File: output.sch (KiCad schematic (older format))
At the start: 12 parts, among them U3 OPA549, U4 INA240A1D, U5 OPA549, U6 INA240A1D

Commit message: Finished first version of schematic
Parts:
- removed R10: R_Shunt, symbol Device:R_Shunt
- added R17: R_Shunt, Resistor_SMD:R_Shunt_Ohmite_LVK12, symbol Device:R_Shunt
- C7: renamed from C14; footprint (none) -> Capacitor_SMD:C_0603_1608Metric
- C8: renamed from C15; footprint (none) -> Capacitor_SMD:C_0603_1608Metric
- R12: renamed from R5; footprint (none) -> Resistor_SMD:R_0603_1608Metric
- R13: renamed from R6; footprint (none) -> Resistor_SMD:R_0603_1608Metric
- R14: renamed from R7; footprint (none) -> Resistor_SMD:R_Shunt_Ohmite_LVK12; OrderN (none) -> LVK12R010DERCT-ND
- R15: renamed from R8; footprint (none) -> Resistor_SMD:R_0603_1608Metric
- R16: renamed from R9; footprint (none) -> Resistor_SMD:R_0603_1608Metric
- renumbered U3 to U1, U4 to U2, U5 to U3, U6 to U4
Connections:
- net SENSE_4T_1: now also R17.4
- net SENSE_4T_2: now also R17.1
- net at U4.1 (-): now also R17.3
- net at U4.8 (+): now also R17.2
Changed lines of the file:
@@
 $Descr A4 11693 8268
 encoding utf-8
-Sheet 3 4
-Title ""
-Date ""
-Rev ""
-Comp ""
+Sheet 2 5
+Title "Z Sim"
+Date "2019-10-22"
+Rev "0.1"
+Comp "ELp"
 Comment1 ""
 Comment2 ""
@@
 $EndDescr
 $Comp
-L rise_elp:OPA549 U3
+L rise_elp:OPA549 U1
 U 1 1 5DADB292
 P 2500 3250
-F 0 "U3" H 2750 3550 50  0000 L CNN
+F 0 "U1" H 2750 3550 50  0000 L CNN
 F 1 "OPA549" H 2400 3250 50  0000 L CNN
 F 2 "Package_TO_SOT_THT:TO-220-11_P3.4x5.08mm_StaggerOdd_Lead4.85mm_Vertical" H 2500 3250 50  0001 C CNN
@@
 	2450 2600 2450 2800
 $Comp
-L power:GND #PWR0120
+L power:GND #PWR014
 U 1 1 5DADB93D
 P 2450 4250
-F 0 "#PWR0120" H 2450 4000 50  0001 C CNN
+F 0 "#PWR014" H 2450 4000 50  0001 C CNN
 F 1 "GND" H 2455 4077 50  0000 C CNN
 F 2 "" H 2450 4250 50  0001 C CNN
@@
 V_OUT1
 $Comp
-L Device:R_Small R6
+L Device:R_Small R13
 U 1 1 5DADC336
 P 1400 3450
-F 0 "R6" H 1459 3496 50  0000 L CNN
+F 0 "R13" H 1459 3496 50  0000 L CNN
 F 1 "10k" H 1459 3405 50  0000 L CNN
-F 2 "" H 1400 3450 50  0001 C CNN
+F 2 "Resistor_SMD:R_0603_1608Metric" H 1400 3450 50  0001 C CNN
 F 3 "~" H 1400 3450 50  0001 C CNN
 	1    1400 3450
@@
 $EndComp
 $Comp
-L Device:R_Small R5
+L Device:R_Small R12
 U 1 1 5DADCC5D
 P 1400 2700
-F 0 "R5" H 1459 2746 50  0000 L CNN
+F 0 "R12" H 1459 2746 50  0000 L CNN
 F 1 "10k" H 1459 2655 50  0000 L CNN
-F 2 "" H 1400 2700 50  0001 C CNN
+F 2 "Resistor_SMD:R_0603_1608Metric" H 1400 2700 50  0001 C CNN
 F 3 "~" H 1400 2700 50  0001 C CNN
 	1    1400 2700
@@
 ES1
 $Comp
-L Device:R_Shunt R7
+L Device:R_Shunt R14
 U 1 1 5DADFAE8
 P 3750 3200
-F 0 "R7" V 3525 3200 50  0000 C CNN
+F 0 "R14" V 3525 3200 50  0000 C CNN
 F 1 "R_Shunt" V 3616 3200 50  0000 C CNN
-F 2 "" V 3680 3200 50  0001 C CNN
+F 2 "Resistor_SMD:R_Shunt_Ohmite_LVK12" V 3680 3200 50  0001 C CNN
 F 3 "~" H 3750 3200 50  0001 C CNN
+F 4 "LVK12R010DERCT-ND" V 3750 3200 50  0001 C CNN "OrderN"
 	1    3750 3200
 	0    1    1    0
@@
 	3350 3300 3150 3300
 $Comp
-L Amplifier_Current:INA240A1D U4
+L Amplifier_Current:INA240A1D U2
 U 1 1 5DAE1093
 P 3750 3900
-F 0 "U4" V 3750 4050 50  0000 L CNN
+F 0 "U2" V 3750 4050 50  0000 L CNN
 F 1 "INA240A1D" V 3850 4050 50  0000 L CNN
 F 2 "Package_SO:SOIC-8_3.9x4.9mm_P1.27mm" H 3750 3250 50  0001 C CNN
@@
 	3350 3800 3450 3800
 $Comp
-L power:GND #PWR0121
+L power:GND #PWR015
 U 1 1 5DAE8C45
 P 3350 4100
-F 0 "#PWR0121" H 3350 3850 50  0001 C CNN
+F 0 "#PWR015" H 3350 3850 50  0001 C CNN
 F 1 "GND" H 3355 3927 50  0000 C CNN
 F 2 "" H 3350 4100 50  0001 C CNN
@@
 Connection ~ 4250 3500
 $Comp
-L Device:C_Small C14
+L Device:C_Small C7
 U 1 1 5DAE9B2D
 P 3150 3850
-F 0 "C14" H 3000 3750 50  0000 L CNN
+F 0 "C7" H 3000 3750 50  0000 L CNN
 F 1 "2.2u" H 2950 3950 50  0000 L CNN
-F 2 "" H 3150 3850 50  0001 C CNN
+F 2 "Capacitor_SMD:C_0603_1608Metric" H 3150 3850 50  0001 C CNN
 F 3 "~" H 3150 3850 50  0001 C CNN
 	1    3150 3850
@@
 Connection ~ 3250 3500
 $Comp
-L power:+3.3VA #PWR0122
+L power:+3.3VA #PWR016
 U 1 1 5DAE93D3
 P 4250 3400
-F 0 "#PWR0122" H 4250 3250 50  0001 C CNN
+F 0 "#PWR016" H 4250 3250 50  0001 C CNN
 F 1 "+3.3VA" H 4050 3450 50  0000 C CNN
 F 2 "" H 4250 3400 50  0001 C CNN
@@
 	5750 3200 5550 3200
 $Comp
-L power:GND #PWR0123
+L power:GND #PWR017
 U 1 1 5DAEEBB5
 P 6450 4250
-F 0 "#PWR0123" H 6450 4000 50  0001 C CNN
+F 0 "#PWR017" H 6450 4000 50  0001 C CNN
 F 1 "GND" H 6455 4077 50  0000 C CNN
 F 2 "" H 6450 4250 50  0001 C CNN
@@
 	6350 2850 6350 2600
 $Comp
-L rise_elp:OPA549 U5
+L rise_elp:OPA549 U3
 U 1 1 5DAEEBCF
 P 6400 3250
-F 0 "U5" H 6650 3550 50  0000 L CNN
+F 0 "U3" H 6650 3550 50  0000 L CNN
 F 1 "OPA549" H 6300 3250 50  0000 L CNN
 F 2 "Package_TO_SOT_THT:TO-220-11_P3.4x5.08mm_StaggerOdd_Lead4.85mm_Vertical" H 6400 3250 50  0001 C CNN
@@
 	6450 4250 6450 4100
 $Comp
-L Device:R_Small R9
+L Device:R_Small R16
 U 1 1 5DAEEBA7
 P 7450 3450
-F 0 "R9" H 7509 3496 50  0000 L CNN
+F 0 "R16" H 7509 3496 50  0000 L CNN
 F 1 "10k" H 7509 3405 50  0000 L CNN
-F 2 "" H 7450 3450 50  0001 C CNN
+F 2 "Resistor_SMD:R_0603_1608Metric" H 7450 3450 50  0001 C CNN
 F 3 "~" H 7450 3450 50  0001 C CNN
 	1    7450 3450
@@
 $EndComp
 $Comp
-L Device:R_Small R8
+L Device:R_Small R15
 U 1 1 5DAEEB41
 P 7450 2700
-F 0 "R8" H 7509 2746 50  0000 L CNN
+F 0 "R15" H 7509 2746 50  0000 L CNN
 F 1 "10k" H 7509 2655 50  0000 L CNN
-F 2 "" H 7450 2700 50  0001 C CNN
+F 2 "Resistor_SMD:R_0603_1608Metric" H 7450 2700 50  0001 C CNN
 F 3 "~" H 7450 2700 50  0001 C CNN
 	1    7450 2700
@@
 	9000 3500 9000 3300
 $Comp
-L power:GND #PWR0124
+L power:GND #PWR018
 U 1 1 5DAF9612
 P 9000 3600
-F 0 "#PWR0124" H 9000 3350 50  0001 C CNN
+F 0 "#PWR018" H 9000 3350 50  0001 C CNN
 F 1 "GND" H 9005 3427 50  0000 C CNN
 F 2 "" H 9000 3600 50  0001 C CNN
@@
 	9000 3300 9100 3300
 $Comp
-L Amplifier_Current:INA240A1D U6
+L Amplifier_Current:INA240A1D U4
 U 1 1 5DAF962B
 P 9400 3400
-F 0 "U6" V 9400 3550 50  0000 L CNN
+F 0 "U4" V 9400 3550 50  0000 L CNN
 F 1 "INA240A1D" V 9500 3550 50  0000 L CNN
 F 2 "Package_SO:SOIC-8_3.9x4.9mm_P1.27mm" H 9400 2750 50  0001 C CNN
@@
 	9100 3400 8900 3400
 $Comp
-L Device:C_Small C15
+L Device:C_Small C8
 U 1 1 5DAF963B
 P 8800 3350
-F 0 "C15" H 8650 3250 50  0000 L CNN
+F 0 "C8" H 8650 3250 50  0000 L CNN
 F 1 "2.2u" H 8600 3450 50  0000 L CNN
-F 2 "" H 8800 3350 50  0001 C CNN
+F 2 "Capacitor_SMD:C_0603_1608Metric" H 8800 3350 50  0001 C CNN
 F 3 "~" H 8800 3350 50  0001 C CNN
 	1    8800 3350
@@
 Wire Wire Line
 	9900 2900 9900 3000
-$Comp
-L Device:R_Shunt R10
-U 1 1 5DAF964D
-P 9400 2700
-F 0 "R10" V 9175 2700 50  0000 C CNN
-F 1 "R_Shunt" V 9266 2700 50  0000 C CNN
-F 2 "" V 9330 2700 50  0001 C CNN
-F 3 "~" H 9400 2700 50  0001 C CNN
-	1    9400 2700
-	0    1    1    0
-$EndComp
 Wire Wire Line
 	8900 3400 8900 3000
 $Comp
-L power:+3.3VA #PWR0125
+L power:+3.3VA #PWR019
 U 1 1 5DB044D1
 P 9900 2900
-F 0 "#PWR0125" H 9900 2750 50  0001 C CNN
+F 0 "#PWR019" H 9900 2750 50  0001 C CNN
 F 1 "+3.3VA" H 9700 2950 50  0000 C CNN
 F 2 "" H 9900 2900 50  0001 C CNN
@@
 Text HLabel 9600 2700 2    50   Input ~ 0
 SENSE_4T_2
+$Comp
+L Device:R_Shunt R17
+U 1 1 5DAEC8CF
+P 9400 2700
+F 0 "R17" V 9175 2700 50  0000 C CNN
+F 1 "R_Shunt" V 9266 2700 50  0000 C CNN
+F 2 "Resistor_SMD:R_Shunt_Ohmite_LVK12" V 9330 2700 50  0001 C CNN
+F 3 "~" H 9400 2700 50  0001 C CNN
+F 4 "LVK12R010DERCT-ND" V 9400 2700 50  0001 C CNN "OrderN"
+	1    9400 2700
+	0    1    1    0
+$EndComp
 $EndSCHEMATC

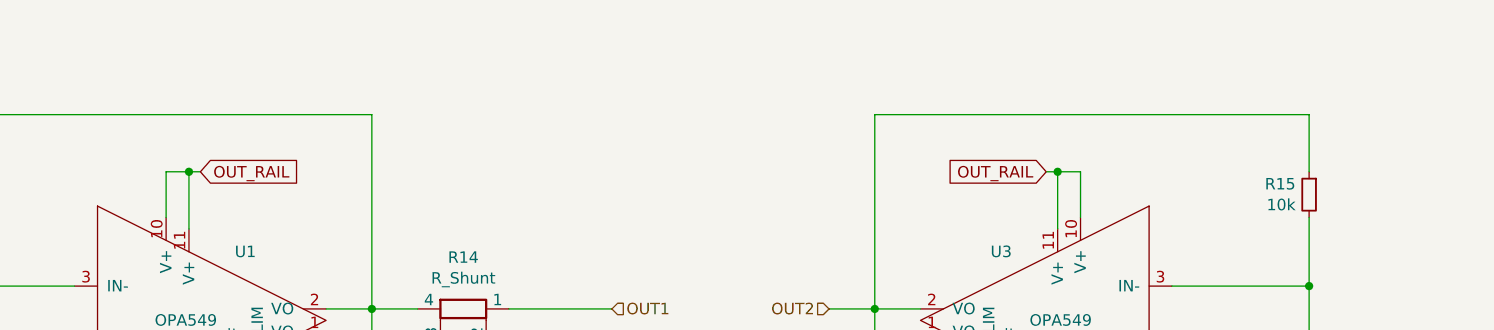
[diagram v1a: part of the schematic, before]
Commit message: preparation for routing and adding kylfläns
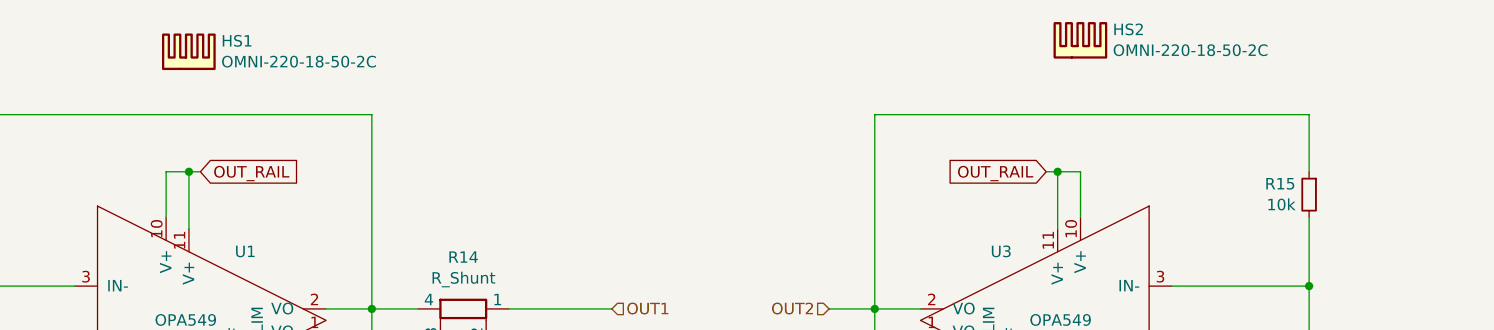
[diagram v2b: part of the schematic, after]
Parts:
- added HS1, HS2: OMNI-220-18-50-2C, rise_elp:OMNI-220-18-50-2C, symbol Mechanical:Heatsink
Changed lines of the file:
@@
 	0    1    1    0
 $EndComp
+$Comp
+L Mechanical:Heatsink HS1
+U 1 1 5DBA0CBC
+P 2550 2150
+F 0 "HS1" H 2691 2271 50  0000 L CNN
+F 1 "OMNI-220-18-50-2C" H 2691 2180 50  0000 L CNN
+F 2 "rise_elp:OMNI-220-18-50-2C" H 2562 2150 50  0001 C CNN
+F 3 "~" H 2562 2150 50  0001 C CNN
+F 4 "345-1491-ND" H 2550 2150 50  0001 C CNN "OrderN"
+	1    2550 2150
+	1    0    0    -1
+$EndComp
+$Comp
+L Mechanical:Heatsink HS2
+U 1 1 5DBA3198
+P 6450 2100
+F 0 "HS2" H 6591 2221 50  0000 L CNN
+F 1 "OMNI-220-18-50-2C" H 6591 2130 50  0000 L CNN
+F 2 "rise_elp:OMNI-220-18-50-2C" H 6462 2100 50  0001 C CNN
+F 3 "~" H 6462 2100 50  0001 C CNN
+F 4 "345-1491-ND" H 6450 2100 50  0001 C CNN "OrderN"
+	1    6450 2100
+	1    0    0    -1
+$EndComp
 $EndSCHEMATC

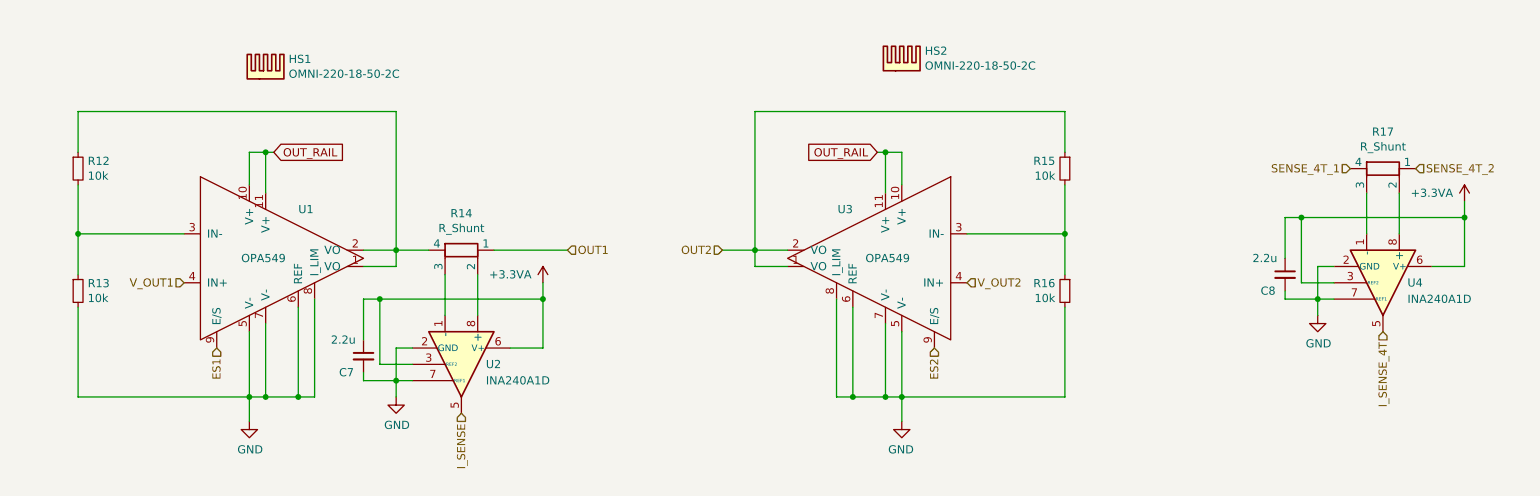
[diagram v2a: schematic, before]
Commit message: Schematic updates, added 3D models and started routing
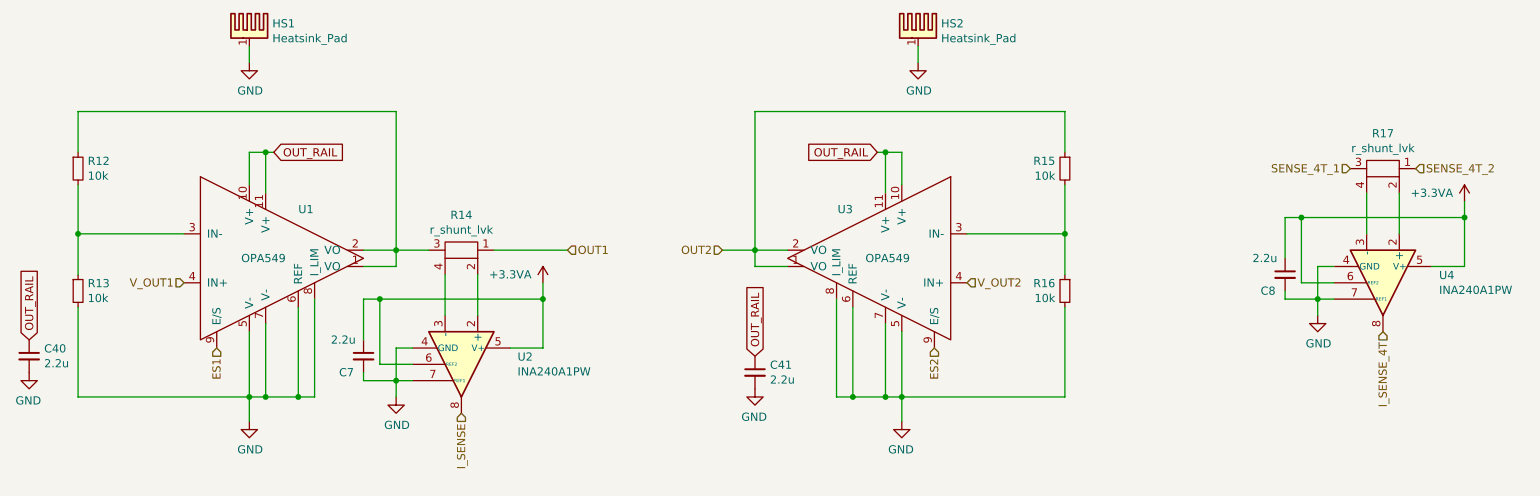
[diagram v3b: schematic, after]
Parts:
- removed HS1, HS2: OMNI-220-18-50-2C, rise_elp:OMNI-220-18-50-2C, symbol Mechanical:Heatsink
- removed R14, R17: R_Shunt, Resistor_SMD:R_Shunt_Ohmite_LVK12, symbol Device:R_Shunt
- removed U2, U4: INA240A1D, Package_SO:SOIC-8_3.9x4.9mm_P1.27mm, symbol Amplifier_Current:INA240A1D
- added C40, C41: 2.2u, Capacitor_SMD:C_0603_1608Metric, symbol Device:C_Small
- added HS1, HS2: Heatsink_Pad, rise_elp:OMNI-220-18-50-2C, symbol Mechanical:Heatsink_Pad
- added R14, R17: r_shunt_lvk, Resistor_SMD:R_Shunt_Ohmite_LVK12, symbol rise_elp:r_shunt_lvk
- added U2, U4: INA240A1PW, Package_SO:TSSOP-8_4.4x3mm_P0.65mm, symbol Amplifier_Current:INA240A1PW
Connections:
- net +3.3VA: now also U2.5 (V+), U2.6 (REF2), U4.5 (V+), U4.6 (REF2)
- net GND: now also C40.2, C41.2, HS1.1, HS2.1, U2.1 (GND), U2.4 (GND), U2.7 (REF1), U4.1 (GND), U4.4 (GND), U4.7 (REF1)
- net I_SENSE: now also U2.8
- net I_SENSE_4T: now also U4.8
- net OUT1: now also R14.1
- net OUT_RAIL: now also C40.1, C41.1
- net SENSE_4T_1: now also R17.3
- net SENSE_4T_2: now also R17.1
- net at R12.1, U1.1 (VO), U1.2 (VO): now also R14.3
- new net: R17.2, U4.2 (+)
- new net: R17.4, U4.3 (-)
- new net: R14.2, U2.2 (+)
- new net: R14.4, U2.3 (-)
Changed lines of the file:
@@
 Text HLabel 2250 3800 3    50   Input ~ 0
 ES1
-$Comp
-L Device:R_Shunt R14
-U 1 1 5DADFAE8
-P 3750 3200
-F 0 "R14" V 3525 3200 50  0000 C CNN
-F 1 "R_Shunt" V 3616 3200 50  0000 C CNN
-F 2 "Resistor_SMD:R_Shunt_Ohmite_LVK12" V 3680 3200 50  0001 C CNN
-F 3 "~" H 3750 3200 50  0001 C CNN
-F 4 "LVK12R010DERCT-ND" V 3750 3200 50  0001 C CNN "OrderN"
-	1    3750 3200
-	0    1    1    0
-$EndComp
 Wire Wire Line
 	3350 3200 3550 3200
@@
 Wire Wire Line
 	3350 3300 3150 3300
-$Comp
-L Amplifier_Current:INA240A1D U2
-U 1 1 5DAE1093
-P 3750 3900
-F 0 "U2" V 3750 4050 50  0000 L CNN
-F 1 "INA240A1D" V 3850 4050 50  0000 L CNN
-F 2 "Package_SO:SOIC-8_3.9x4.9mm_P1.27mm" H 3750 3250 50  0001 C CNN
-F 3 "http://www.ti.com/lit/ds/symlink/ina240.pdf" H 3900 4050 50  0001 C CNN
-F 4 "296-45088-1-ND" V 3750 3900 50  0001 C CNN "OrderN"
-	1    3750 3900
-	0    1    1    0
-$EndComp
 Wire Wire Line
 	3650 3600 3650 3350
@@
 Wire Wire Line
 	9000 3300 9100 3300
-$Comp
-L Amplifier_Current:INA240A1D U4
-U 1 1 5DAF962B
-P 9400 3400
-F 0 "U4" V 9400 3550 50  0000 L CNN
-F 1 "INA240A1D" V 9500 3550 50  0000 L CNN
-F 2 "Package_SO:SOIC-8_3.9x4.9mm_P1.27mm" H 9400 2750 50  0001 C CNN
-F 3 "http://www.ti.com/lit/ds/symlink/ina240.pdf" H 9550 3550 50  0001 C CNN
-F 4 "296-45088-1-ND" V 9400 3400 50  0001 C CNN "OrderN"
-	1    9400 3400
-	0    1    1    0
-$EndComp
 Wire Wire Line
 	9900 3300 9700 3300
@@
 SENSE_4T_2
 $Comp
-L Device:R_Shunt R17
-U 1 1 5DAEC8CF
+L Mechanical:Heatsink_Pad HS1
+U 1 1 5DB19FF5
+P 2450 1850
+F 0 "HS1" H 2591 1889 50  0000 L CNN
+F 1 "Heatsink_Pad" H 2591 1798 50  0000 L CNN
+F 2 "rise_elp:OMNI-220-18-50-2C" H 2462 1800 50  0001 C CNN
+F 3 "~" H 2462 1800 50  0001 C CNN
+F 4 "345-1491-ND" H 2450 1850 50  0001 C CNN "OrderN"
+	1    2450 1850
+	1    0    0    -1
+$EndComp
+$Comp
+L power:GND #PWR05
+U 1 1 5DB1A98E
+P 2450 2050
+F 0 "#PWR05" H 2450 1800 50  0001 C CNN
+F 1 "GND" H 2455 1877 50  0000 C CNN
+F 2 "" H 2450 2050 50  0001 C CNN
+F 3 "" H 2450 2050 50  0001 C CNN
+	1    2450 2050
+	1    0    0    -1
+$EndComp
+Wire Wire Line
+	2450 2050 2450 1950
+$Comp
+L power:GND #PWR07
+U 1 1 5DB1AF31
+P 6550 2050
+F 0 "#PWR07" H 6550 1800 50  0001 C CNN
+F 1 "GND" H 6555 1877 50  0000 C CNN
+F 2 "" H 6550 2050 50  0001 C CNN
+F 3 "" H 6550 2050 50  0001 C CNN
+	1    6550 2050
+	1    0    0    -1
+$EndComp
+Wire Wire Line
+	6550 2050 6550 1950
+$Comp
+L Mechanical:Heatsink_Pad HS2
+U 1 1 5DB1AF40
+P 6550 1850
+F 0 "HS2" H 6691 1889 50  0000 L CNN
+F 1 "Heatsink_Pad" H 6691 1798 50  0000 L CNN
+F 2 "rise_elp:OMNI-220-18-50-2C" H 6562 1800 50  0001 C CNN
+F 3 "~" H 6562 1800 50  0001 C CNN
+F 4 "345-1491-ND" H 6550 1850 50  0001 C CNN "OrderN"
+	1    6550 1850
+	1    0    0    -1
+$EndComp
+$Comp
+L rise_elp:r_shunt_lvk R17
+U 1 1 5DB24C5C
 P 9400 2700
-F 0 "R17" V 9175 2700 50  0000 C CNN
-F 1 "R_Shunt" V 9266 2700 50  0000 C CNN
-F 2 "Resistor_SMD:R_Shunt_Ohmite_LVK12" V 9330 2700 50  0001 C CNN
-F 3 "~" H 9400 2700 50  0001 C CNN
+F 0 "R17" V 9185 2700 50  0000 C CNN
+F 1 "r_shunt_lvk" V 9276 2700 50  0000 C CNN
+F 2 "Resistor_SMD:R_Shunt_Ohmite_LVK12" H 9400 2700 50  0001 C CNN
+F 3 "" H 9400 2700 50  0001 C CNN
 F 4 "LVK12R010DERCT-ND" V 9400 2700 50  0001 C CNN "OrderN"
 	1    9400 2700
@@
 $EndComp
 $Comp
-L Mechanical:Heatsink HS1
-U 1 1 5DBA0CBC
-P 2550 2150
-F 0 "HS1" H 2691 2271 50  0000 L CNN
-F 1 "OMNI-220-18-50-2C" H 2691 2180 50  0000 L CNN
-F 2 "rise_elp:OMNI-220-18-50-2C" H 2562 2150 50  0001 C CNN
-F 3 "~" H 2562 2150 50  0001 C CNN
-F 4 "345-1491-ND" H 2550 2150 50  0001 C CNN "OrderN"
-	1    2550 2150
-	1    0    0    -1
-$EndComp
-$Comp
-L Mechanical:Heatsink HS2
-U 1 1 5DBA3198
-P 6450 2100
-F 0 "HS2" H 6591 2221 50  0000 L CNN
-F 1 "OMNI-220-18-50-2C" H 6591 2130 50  0000 L CNN
-F 2 "rise_elp:OMNI-220-18-50-2C" H 6462 2100 50  0001 C CNN
-F 3 "~" H 6462 2100 50  0001 C CNN
-F 4 "345-1491-ND" H 6450 2100 50  0001 C CNN "OrderN"
-	1    6450 2100
-	1    0    0    -1
+L rise_elp:r_shunt_lvk R14
+U 1 1 5DB2B675
+P 3750 3200
+F 0 "R14" V 3535 3200 50  0000 C CNN
+F 1 "r_shunt_lvk" V 3626 3200 50  0000 C CNN
+F 2 "Resistor_SMD:R_Shunt_Ohmite_LVK12" H 3750 3200 50  0001 C CNN
+F 3 "" H 3750 3200 50  0001 C CNN
+F 4 "LVK12R010DERCT-ND" V 3750 3200 50  0001 C CNN "OrderN"
+	1    3750 3200
+	0    1    1    0
+$EndComp
+$Comp
+L Device:C_Small C41
+U 1 1 5DB35792
+P 5550 3950
+F 0 "C41" H 5642 3996 50  0000 L CNN
+F 1 "2.2u" H 5642 3905 50  0000 L CNN
+F 2 "Capacitor_SMD:C_0603_1608Metric" H 5550 3950 50  0001 C CNN
+F 3 "~" H 5550 3950 50  0001 C CNN
+	1    5550 3950
+	1    0    0    -1
+$EndComp
+Text GLabel 5550 3850 1    50   Input ~ 0
+OUT_RAIL
+$Comp
+L power:GND #PWR09
+U 1 1 5DB329D3
+P 5550 4050
+F 0 "#PWR09" H 5550 3800 50  0001 C CNN
+F 1 "GND" H 5555 3877 50  0000 C CNN
+F 2 "" H 5550 4050 50  0001 C CNN
+F 3 "" H 5550 4050 50  0001 C CNN
+	1    5550 4050
+	-1   0    0    -1
+$EndComp
+$Comp
+L Device:C_Small C40
+U 1 1 5DB32F4D
+P 1100 3850
+F 0 "C40" H 1192 3896 50  0000 L CNN
+F 1 "2.2u" H 1192 3805 50  0000 L CNN
+F 2 "Capacitor_SMD:C_0603_1608Metric" H 1100 3850 50  0001 C CNN
+F 3 "~" H 1100 3850 50  0001 C CNN
+	1    1100 3850
+	1    0    0    -1
+$EndComp
+$Comp
+L power:GND #PWR08
+U 1 1 5DB32F5A
+P 1100 3950
+F 0 "#PWR08" H 1100 3700 50  0001 C CNN
+F 1 "GND" H 1105 3777 50  0000 C CNN
+F 2 "" H 1100 3950 50  0001 C CNN
+F 3 "" H 1100 3950 50  0001 C CNN
+	1    1100 3950
+	-1   0    0    -1
+$EndComp
+Text GLabel 1100 3750 1    50   Input ~ 0
+OUT_RAIL
+$Comp
+L Amplifier_Current:INA240A1PW U2
+U 1 1 5DB685A0
+P 3750 3900
+F 0 "U2" V 3704 4244 50  0000 L CNN
+F 1 "INA240A1PW" V 3795 4244 50  0000 L CNN
+F 2 "Package_SO:TSSOP-8_4.4x3mm_P0.65mm" H 3750 3250 50  0001 C CNN
+F 3 "http://www.ti.com/lit/ds/symlink/ina240.pdf" H 3900 4050 50  0001 C CNN
+	1    3750 3900
+	0    1    1    0
+$EndComp
+$Comp
+L Amplifier_Current:INA240A1PW U4
+U 1 1 5DB6B0DC
+P 9400 3400
+F 0 "U4" V 9354 3744 50  0000 L CNN
+F 1 "INA240A1PW" V 9445 3744 50  0000 L CNN
+F 2 "Package_SO:TSSOP-8_4.4x3mm_P0.65mm" H 9400 2750 50  0001 C CNN
+F 3 "http://www.ti.com/lit/ds/symlink/ina240.pdf" H 9550 3550 50  0001 C CNN
+	1    9400 3400
+	0    1    1    0
 $EndComp
 $EndSCHEMATC

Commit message: almost done with bom. there are some issues
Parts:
- C40, C41, C7, C8: OrderN (none) -> 490-10731-1-ND
- R12, R13, R15, R16: OrderN (none) -> 311-10.0KHRCT-ND
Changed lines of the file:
@@
 F 2 "Resistor_SMD:R_0603_1608Metric" H 1400 3450 50  0001 C CNN
 F 3 "~" H 1400 3450 50  0001 C CNN
+F 4 " 311-10.0KHRCT-ND" H 1400 3450 50  0001 C CNN "OrderN"
 	1    1400 3450
 	1    0    0    -1
@@
 F 2 "Resistor_SMD:R_0603_1608Metric" H 1400 2700 50  0001 C CNN
 F 3 "~" H 1400 2700 50  0001 C CNN
+F 4 " 311-10.0KHRCT-ND" H 1400 2700 50  0001 C CNN "OrderN"
 	1    1400 2700
 	1    0    0    -1
@@
 F 2 "Capacitor_SMD:C_0603_1608Metric" H 3150 3850 50  0001 C CNN
 F 3 "~" H 3150 3850 50  0001 C CNN
+F 4 "490-10731-1-ND" H 3150 3850 50  0001 C CNN "OrderN"
 	1    3150 3850
 	1    0    0    -1
@@
 F 2 "Resistor_SMD:R_0603_1608Metric" H 7450 3450 50  0001 C CNN
 F 3 "~" H 7450 3450 50  0001 C CNN
+F 4 " 311-10.0KHRCT-ND" H 7450 3450 50  0001 C CNN "OrderN"
 	1    7450 3450
 	-1   0    0    -1
@@
 F 2 "Resistor_SMD:R_0603_1608Metric" H 7450 2700 50  0001 C CNN
 F 3 "~" H 7450 2700 50  0001 C CNN
+F 4 " 311-10.0KHRCT-ND" H 7450 2700 50  0001 C CNN "OrderN"
 	1    7450 2700
 	-1   0    0    -1
@@
 F 2 "Capacitor_SMD:C_0603_1608Metric" H 8800 3350 50  0001 C CNN
 F 3 "~" H 8800 3350 50  0001 C CNN
+F 4 "490-10731-1-ND" H 8800 3350 50  0001 C CNN "OrderN"
 	1    8800 3350
 	1    0    0    -1
@@
 F 2 "Capacitor_SMD:C_0603_1608Metric" H 5550 3950 50  0001 C CNN
 F 3 "~" H 5550 3950 50  0001 C CNN
+F 4 "490-10731-1-ND" H 5550 3950 50  0001 C CNN "OrderN"
 	1    5550 3950
 	1    0    0    -1
@@
 F 2 "Capacitor_SMD:C_0603_1608Metric" H 1100 3850 50  0001 C CNN
 F 3 "~" H 1100 3850 50  0001 C CNN
+F 4 "490-10731-1-ND" H 1100 3850 50  0001 C CNN "OrderN"
 	1    1100 3850
 	1    0    0    -1
